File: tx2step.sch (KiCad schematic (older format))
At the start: 69 parts, among them CON1 BARREL_JACK, IC1 ATMEGA328P-MM, IC2 DRV8834, IC3 DRV8834, IC4 TPS2113A, IC5 MCP73831, IC6 TPS61202, J1 RJ45, J2 RJ12, J3 RJ12, SW1 SW_DPDT_x2, SW2 SW_SPDT_MSM, SW3 SW_DIP_x02, Y1 16 MHz

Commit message: Remap symbols to new format
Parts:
- BT1: symbol Battery_Cell -> tx2step-rescue:Battery_Cell
- C1, C17, C18: symbol CP_Small -> tx2step-rescue:CP_Small
- C10, C11, C12, C13, C14, C15, C16, C19, C2, C20, C21, C22, C3, C4, C5, C6, C7, C8, C9: symbol C_Small -> tx2step-rescue:C_Small
- CON1: symbol BARREL_JACK -> tx2step-rescue:BARREL_JACK
- D1, D4: symbol LED -> tx2step-rescue:LED
- D10, D7, D8, D9: symbol D_TVS -> tx2step-rescue:D_TVS
- D2, D3: symbol D -> tx2step-rescue:D
- D5, D6: symbol LED_Small -> tx2step-rescue:LED_Small
- IC1: symbol ATMEGA328P-MM -> tx2step-rescue:ATMEGA328P-MM
- IC2, IC3: symbol DRV8834 -> tx2step-rescue:DRV8834
- IC4: symbol TPS2113A -> tx2step-rescue:TPS2113A
- IC5: symbol MCP73831 -> tx2step-rescue:MCP73831
- IC6: symbol TPS61202 -> tx2step-rescue:TPS61202
- J1: symbol RJ45 -> tx2step-rescue:RJ45
- J2, J3: symbol RJ12 -> tx2step-rescue:RJ12
- L1: symbol L -> tx2step-rescue:L
- R1, R10, R11, R12, R13, R14, R15, R16, R17, R18, R19, R2, R20, R3, R4, R5, R6, R7, R8, R9: symbol R_Small -> tx2step-rescue:R_Small
- RV1: symbol POT -> tx2step-rescue:POT
- SW1: symbol SW_DPDT_x2 -> tx2step-rescue:SW_DPDT_x2
- SW2: symbol SW_SPDT_MSM -> tx2step-rescue:SW_SPDT_MSM
- SW3: symbol SW_DIP_x02 -> tx2step-rescue:SW_DIP_x02
- Y1: symbol Crystal -> tx2step-rescue:Crystal
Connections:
- wire segments 264 -> 317

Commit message: Delete +5VL net
Simplify power supply since the TPS2113A auto-muxes the DC input
anyway and just power logic directly from the regulator. Also
avoids running logic off unregulated DC input.
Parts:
- removed D2, D3: D, symbol tx2step-rescue:D
- renumbered C12 to C1, C14 to C10, C8 to C11, C9 to C12, C10 to C13, C11 to C14, C1 to C2, C2 to C3, C3 to C8, C13 to C9, D4 to D2, D5 to D3, D6 to D4, D7 to D5, D8 to D6, D9 to D7, D10 to D8, IC4 to IC1, IC1 to IC2, IC5 to IC3, IC6 to IC4, IC2 to IC5, IC3 to IC6, SW3 to SW1, SW1 to SW2, SW2 to SW3
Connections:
- net labels removed: +5VL
- wire segments 317 -> 309

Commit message: Fix barrel jack connection
GND was connected to wrong barrel jack pin. Connect to both the
sleeve (pin 2) and the switch (pin 3) as we don't actually use
the switch functionality.
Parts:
- CON1: symbol tx2step-rescue:BARREL_JACK -> Connector:Barrel_Jack_Switch
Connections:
- wire segments 309 -> 308
- no-connect marks 14 -> 13
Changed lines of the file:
@@
 $EndComp
 $Comp
-L tx2step-rescue:BARREL_JACK CON1
+L Connector:Barrel_Jack_Switch CON1
 U 1 1 58BAF2CD
-P 1100 1150
-F 0 "CON1" H 1100 1400 50  0000 C CNN
-F 1 "BARREL_JACK" H 1100 950 50  0000 C CNN
-F 2 "" H 1100 1150 50  0000 C CNN
-F 3 "" H 1100 1150 50  0000 C CNN
-	1    1100 1150
+P 1100 1100
+F 0 "CON1" H 1100 1350 50  0000 C CNN
+F 1 "BARREL_JACK" H 1100 900 50  0000 C CNN
+F 2 "" H 1100 1100 50  0000 C CNN
+F 3 "" H 1100 1100 50  0000 C CNN
+	1    1100 1100
 	1    0    0    -1
 $EndComp
@@
 	2700 2550 2850 2550
 Wire Wire Line
-	1400 1050 1400 1000
-Wire Wire Line
 	1400 1000 1600 1000
 Wire Wire Line
 	1600 1200 1400 1200
-Wire Wire Line
-	1400 1200 1400 1150
 Wire Wire Line
 	1600 1200 1600 1300
@@
 NoConn ~ 9400 4600
 NoConn ~ 6200 4050
-NoConn ~ 1400 1250
 Wire Wire Line
 	8750 1850 9400 1850
@@
 	1    0    0    -1
 $EndComp
+Connection ~ 1400 1200
+Wire Wire Line
+	1400 1100 1400 1200
 $EndSCHEMATC

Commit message: Use unshielded jacks
Reduces number of NC pins
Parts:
- J1: value RJ45 -> 8P8C; symbol tx2step-rescue:RJ45 -> Connector:8P8C
- J2, J3: value RJ12 -> 6P4C; symbol tx2step-rescue:RJ12 -> Connector:6P4C
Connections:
- no-connect marks 13 -> 4
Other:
- moved on the sheet: J1

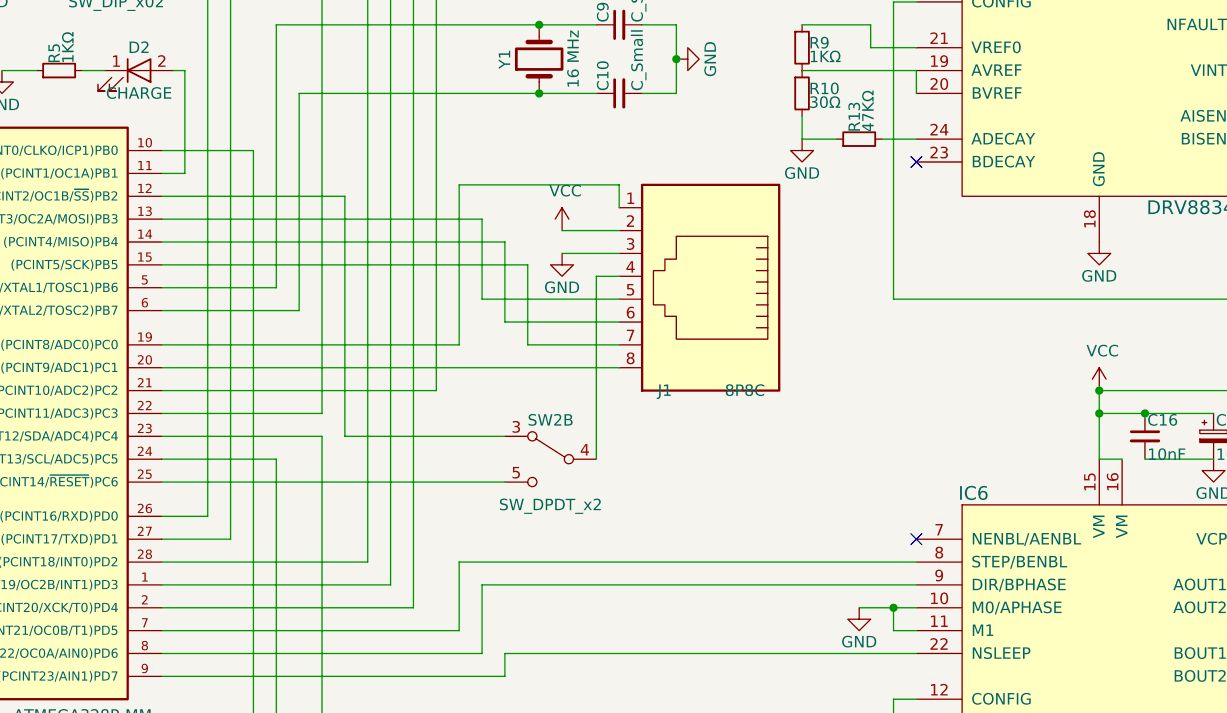
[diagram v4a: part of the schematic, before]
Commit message: Remove debug mode switch
Add an edge connector debug interface rather than overloading the
remote connector for reprogramming.
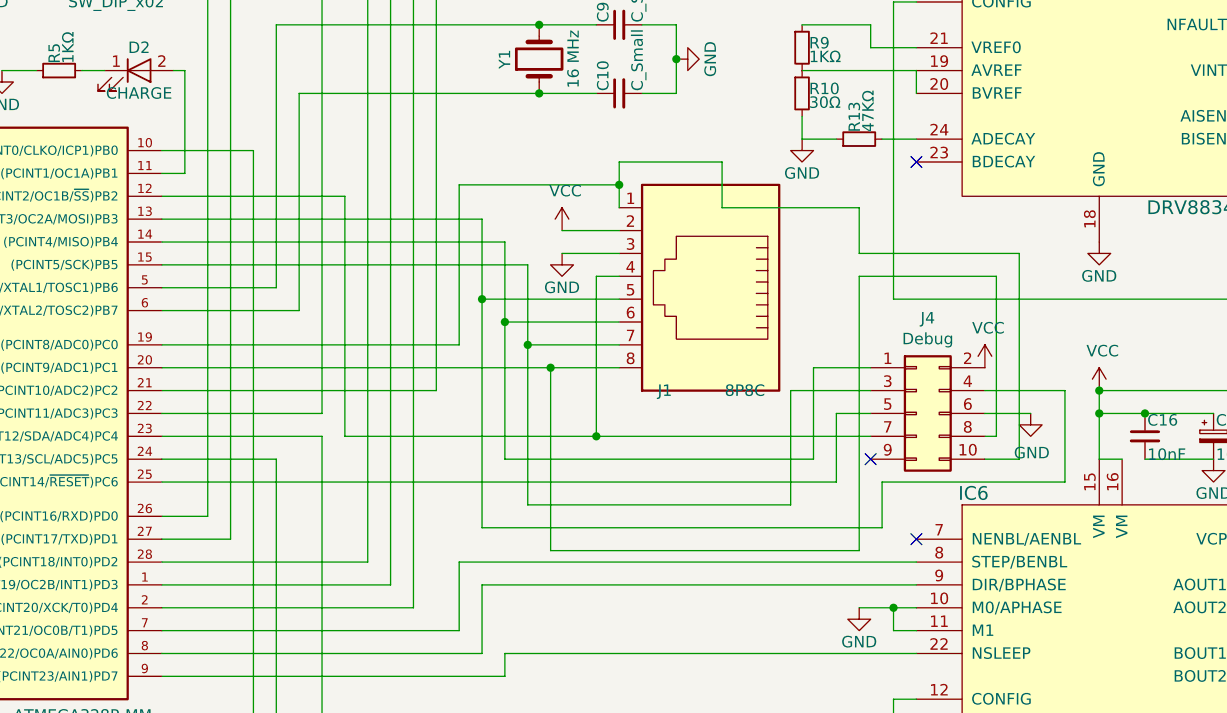
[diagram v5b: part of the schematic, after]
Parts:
- removed unit 2 of SW2
- added J4: Debug, symbol Connector_Generic:Conn_02x05_Odd_Even
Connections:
- net GND: now also J4.6 (Pin_6)
- net VCC: now also J4.2 (Pin_2)
- net at IC2.12 ((PCINT2/OC1B/~SS~)PB2): now also J1.4, J4.7 (Pin_7)
- net at IC2.13 ((PCINT3/OC2A/MOSI)PB3), J1.5: now also J4.4 (Pin_4)
- net at IC2.14 ((PCINT4/MISO)PB4), J1.6: now also J4.1 (Pin_1)
- net at IC2.15 ((PCINT5/SCK)PB5), J1.7: now also J4.3 (Pin_3)
- net at IC2.19 ((PCINT8/ADC0)PC0), J1.1: now also J4.10 (Pin_10)
- net at IC2.20 ((PCINT9/ADC1)PC1), J1.8: now also J4.8 (Pin_8)
- net at IC2.25 ((PCINT14/~RESET~)PC6): now also J4.5 (Pin_5)
- no-connect marks 4 -> 5
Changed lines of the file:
@@
 	4700 3050 4700 3750
 Wire Wire Line
-	5400 3850 3400 3850
+	5400 3850 5100 3850
 Wire Wire Line
 	3400 3300 4900 3300
@@
 Wire Wire Line
 	4200 3100 4200 4150
-Wire Wire Line
-	3400 4350 4900 4350
 Wire Wire Line
 	1500 5100 1350 5100
@@
 	9500 5500 9750 5500
 Wire Wire Line
-	5300 3450 5300 4250
-Wire Wire Line
-	4200 4150 4900 4150
-$Comp
-L tx2step-rescue:SW_DPDT_x2 SW2
-U 2 1 58B50C38
-P 5100 4250
-F 0 "SW2" H 5100 4420 50  0000 C CNN
-F 1 "SW_DPDT_x2" H 5100 4050 50  0000 C CNN
-F 2 "" H 5100 4250 50  0001 C CNN
-F 3 "" H 5100 4250 50  0001 C CNN
-	2    5100 4250
-	-1   0    0    -1
-$EndComp
+	5300 3450 5300 4150
+$Comp
+L power:VCC #PWR042
+U 1 1 5F99EDAE
+P 7000 3850
+F 0 "#PWR042" H 7000 3700 50  0001 C CNN
+F 1 "VCC" H 7015 4023 50  0000 C CNN
+F 2 "" H 7000 3850 50  0001 C CNN
+F 3 "" H 7000 3850 50  0001 C CNN
+	1    7000 3850
+	1    0    0    -1
+$EndComp
+$Comp
+L power:GND #PWR043
+U 1 1 5F9BDCC4
+P 7200 4050
+F 0 "#PWR043" H 7200 3800 50  0001 C CNN
+F 1 "GND" H 7205 3877 50  0000 C CNN
+F 2 "" H 7200 4050 50  0001 C CNN
+F 3 "" H 7200 4050 50  0001 C CNN
+	1    7200 4050
+	1    0    0    -1
+$EndComp
+NoConn ~ 6500 4250
+Wire Wire Line
+	4200 4150 5300 4150
+Wire Wire Line
+	5000 3750 5000 4450
+Connection ~ 5000 3750
+$Comp
+L Connector_Generic:Conn_02x05_Odd_Even J4
+U 1 1 5F99676C
+P 6700 4050
+F 0 "J4" H 6750 4467 50  0000 C CNN
+F 1 "Debug" H 6750 4376 50  0000 C CNN
+F 2 "" H 6700 4050 50  0001 C CNN
+F 3 "~" H 6700 4050 50  0001 C CNN
+	1    6700 4050
+	1    0    0    -1
+$EndComp
+Wire Wire Line
+	6350 4050 6350 4350
+Wire Wire Line
+	6150 4450 6150 3950
+Wire Wire Line
+	5000 4450 6150 4450
+Wire Wire Line
+	4900 3650 4900 4250
+Wire Wire Line
+	6250 4250 6250 3850
+Connection ~ 4900 3650
+Wire Wire Line
+	7000 4050 7200 4050
+Wire Wire Line
+	4900 4250 6250 4250
+Wire Wire Line
+	3400 4350 6350 4350
+Wire Wire Line
+	6350 4050 6500 4050
+Wire Wire Line
+	6150 3950 6500 3950
+Wire Wire Line
+	6250 3850 6500 3850
+Wire Wire Line
+	4800 3550 4800 4550
+Wire Wire Line
+	4800 4550 6550 4550
+Wire Wire Line
+	6550 4550 6550 4350
+Wire Wire Line
+	6550 4350 7350 4350
+Wire Wire Line
+	7350 4350 7350 3950
+Wire Wire Line
+	7350 3950 7000 3950
+Connection ~ 4800 3550
+Wire Wire Line
+	5300 4150 6500 4150
+Connection ~ 5300 4150
+Wire Wire Line
+	5100 3850 5100 4650
+Wire Wire Line
+	5100 4650 6450 4650
+Wire Wire Line
+	6450 4650 6450 3450
+Wire Wire Line
+	6450 3450 7050 3450
+Wire Wire Line
+	7050 3450 7050 4150
+Wire Wire Line
+	7050 4150 7000 4150
+Connection ~ 5100 3850
+Wire Wire Line
+	5100 3850 3400 3850
+Wire Wire Line
+	5400 3050 5400 2950
+Wire Wire Line
+	5400 2950 5850 2950
+Wire Wire Line
+	5850 2950 5850 3150
+Wire Wire Line
+	5850 3150 6450 3150
+Wire Wire Line
+	6450 3150 6450 3350
+Wire Wire Line
+	6450 3350 7150 3350
+Wire Wire Line
+	7150 3350 7150 4250
+Wire Wire Line
+	7150 4250 7000 4250
+Connection ~ 5400 3050
 $EndSCHEMATC
